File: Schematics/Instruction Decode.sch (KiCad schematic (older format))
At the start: 10 parts, among them U52 GLS29EE010, U53 GLS29EE010, U54 74F574, U55 74F574, U56 74F574

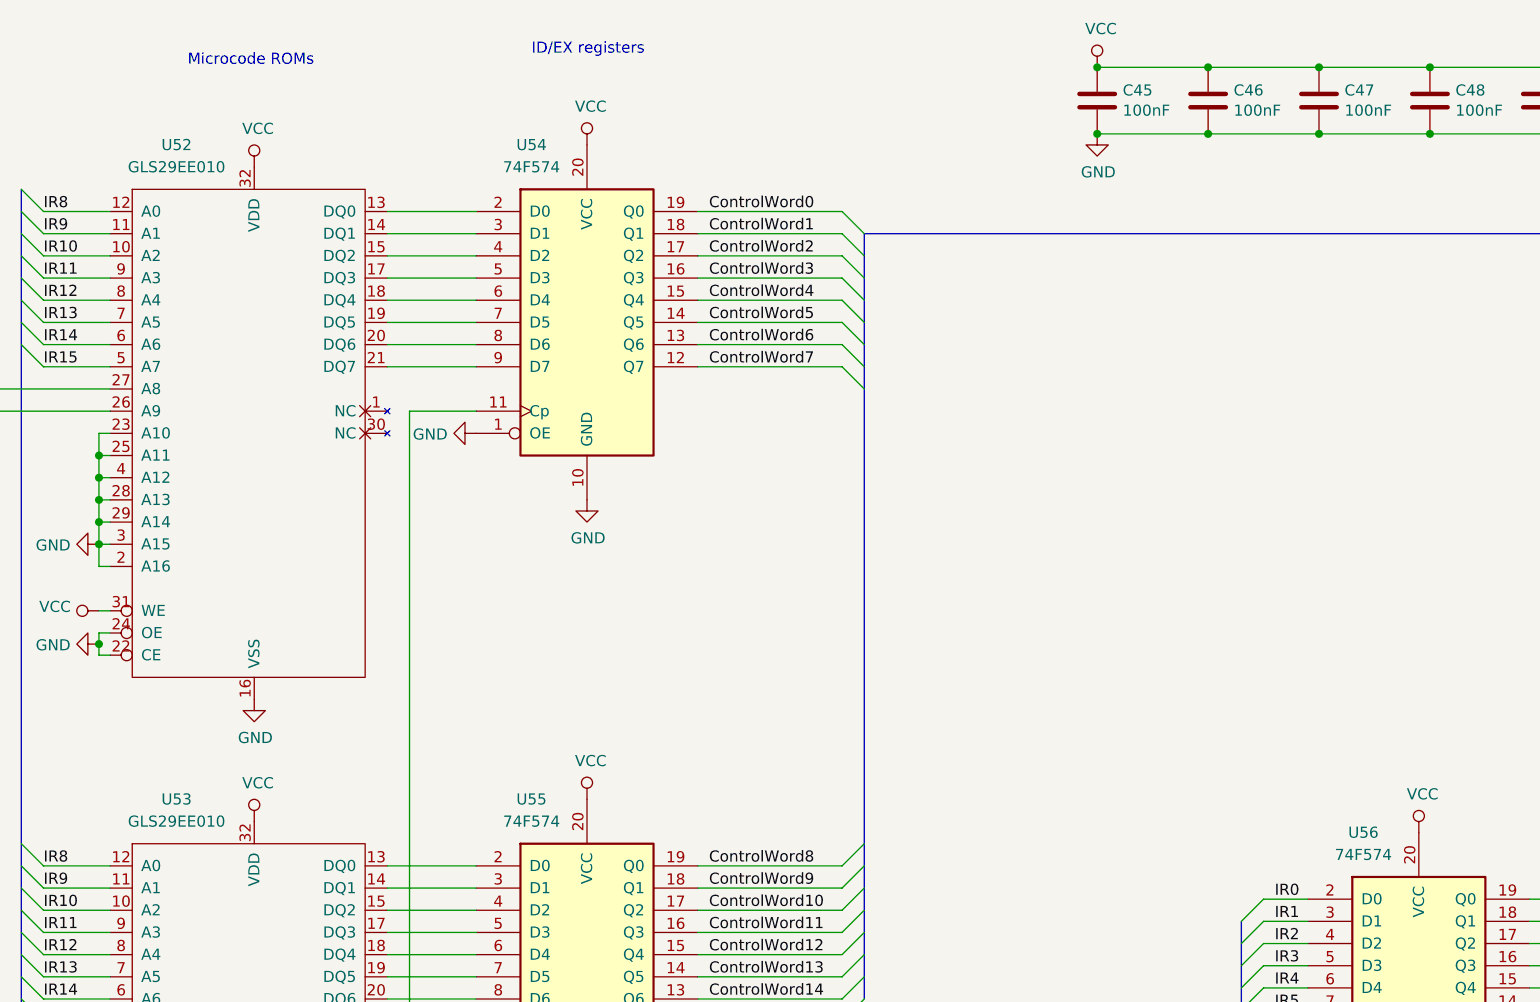
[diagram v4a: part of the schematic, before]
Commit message: Add unused IC units to Output Display to ensure no ICs are shared with other modules.
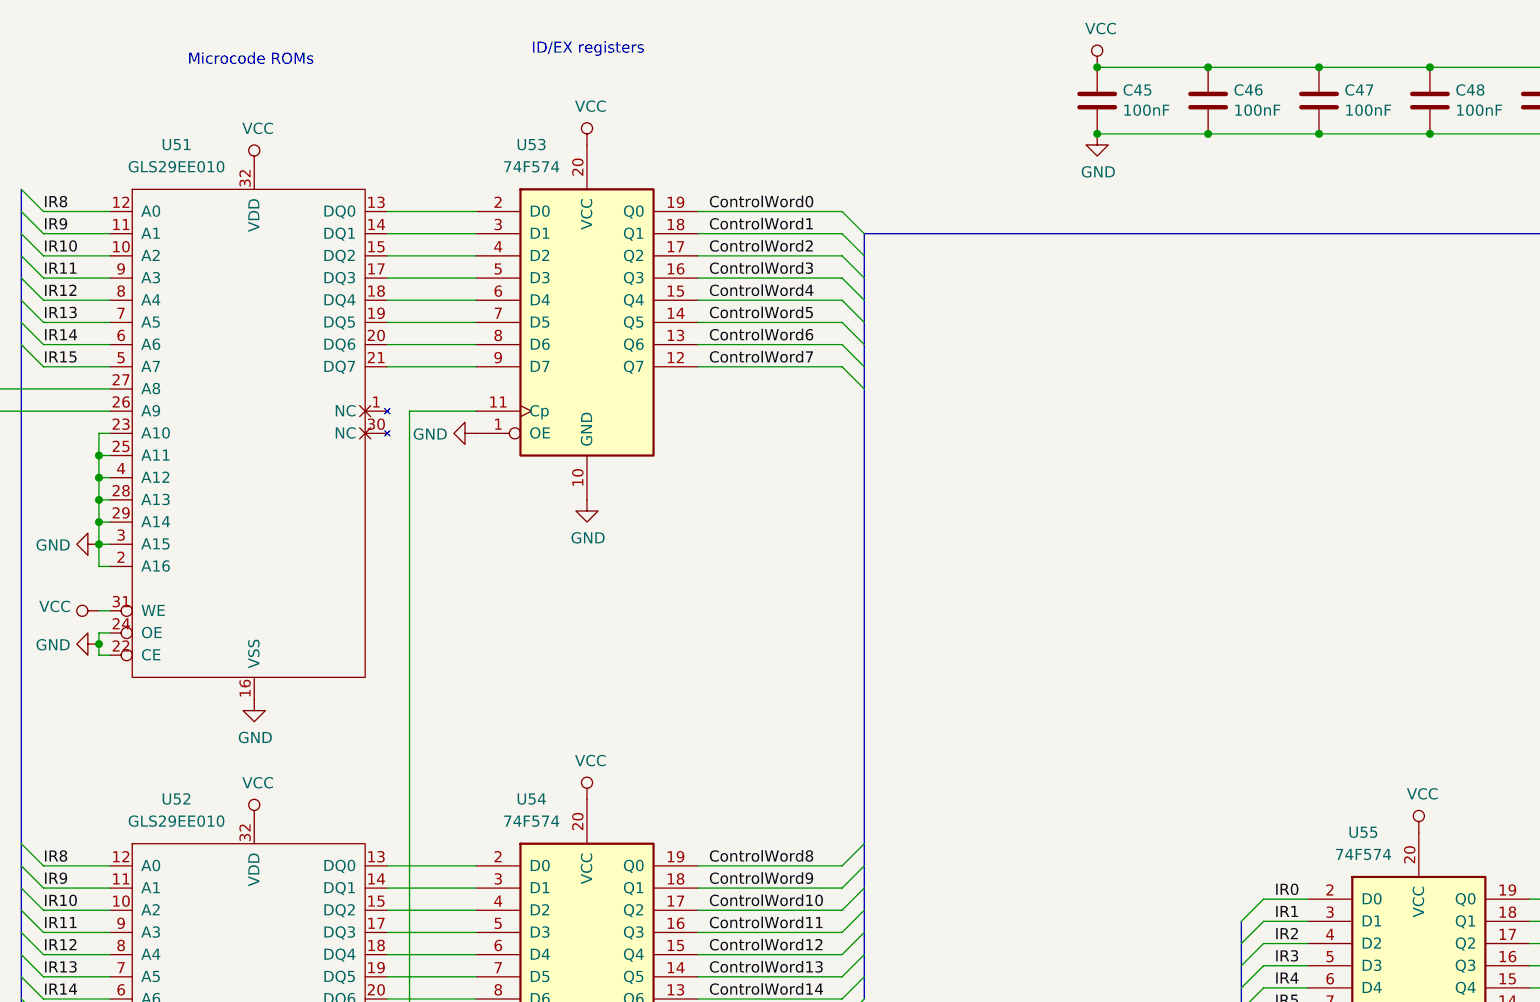
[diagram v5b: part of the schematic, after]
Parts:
- renumbered U52 to U51, U53 to U52, U54 to U53, U55 to U54, U56 to U55
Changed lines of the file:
@@
 P 2900 1250
 AR Path="/5D2C0AA0/5DB5EC09" Ref="U?"  Part="1"
-AR Path="/5D2C0B92/5DB5EC09" Ref="U52"  Part="1"
-F 0 "U52" H 2550 1450 50  0000 C CNN
+AR Path="/5D2C0B92/5DB5EC09" Ref="U51"  Part="1"
+F 0 "U51" H 2550 1450 50  0000 C CNN
 F 1 "GLS29EE010" H 2550 1350 50  0000 C CNN
 F 2 "Package_DIP:DIP-32_W15.24mm_Socket" H 2900 1250 50  0001 C CNN
@@
 P 2900 4200
 AR Path="/5D2C0AA0/5DB5EC5B" Ref="U?"  Part="1"
-AR Path="/5D2C0B92/5DB5EC5B" Ref="U53"  Part="1"
-F 0 "U53" H 2550 4400 50  0000 C CNN
+AR Path="/5D2C0B92/5DB5EC5B" Ref="U52"  Part="1"
+F 0 "U52" H 2550 4400 50  0000 C CNN
 F 1 "GLS29EE010" H 2550 4300 50  0000 C CNN
 F 2 "Package_DIP:DIP-32_W15.24mm_Socket" H 2900 4200 50  0001 C CNN
@@
 P 8150 4950
 AR Path="/5D2C14C3/5DB613F7" Ref="U?"  Part="1"
-AR Path="/5D2C0B92/5DB613F7" Ref="U56"  Part="1"
-F 0 "U56" H 7900 5750 50  0000 C CNN
+AR Path="/5D2C0B92/5DB613F7" Ref="U55"  Part="1"
+F 0 "U55" H 7900 5750 50  0000 C CNN
 F 1 "74F574" H 7900 5650 50  0000 C CNN
 F 2 "Package_DIP:DIP-20_W7.62mm" H 8150 4950 50  0001 C CNN
@@
 $EndComp
 $Comp
-L power:GND #PWR0213
+L power:GND #PWR0133
 U 1 1 5DB6758A
 P 8150 5750
-F 0 "#PWR0213" H 8150 5500 50  0001 C CNN
+F 0 "#PWR0133" H 8150 5500 50  0001 C CNN
 F 1 "GND" H 8155 5577 50  0000 C CNN
 F 2 "" H 8150 5750 50  0001 C CNN
@@
 $EndComp
 $Comp
-L power:VCC #PWR0214
+L power:VCC #PWR0132
 U 1 1 5DB6804E
 P 8150 4150
-F 0 "#PWR0214" H 8150 4000 50  0001 C CNN
+F 0 "#PWR0132" H 8150 4000 50  0001 C CNN
 F 1 "VCC" H 8167 4323 50  0000 C CNN
 F 2 "" H 8150 4150 50  0001 C CNN
@@
 ControlClock
 $Comp
-L power:GND #PWR0215
+L power:GND #PWR0131
 U 1 1 5DB73C30
 P 7650 5450
-F 0 "#PWR0215" H 7650 5200 50  0001 C CNN
+F 0 "#PWR0131" H 7650 5200 50  0001 C CNN
 F 1 "GND" V 7655 5322 50  0000 R CNN
 F 2 "" H 7650 5450 50  0001 C CNN
@@
 P 4400 1850
 AR Path="/5D2C14C3/5DB75B66" Ref="U?"  Part="1"
-AR Path="/5D2C0B92/5DB75B66" Ref="U54"  Part="1"
-F 0 "U54" H 4150 2650 50  0000 C CNN
+AR Path="/5D2C0B92/5DB75B66" Ref="U53"  Part="1"
+F 0 "U53" H 4150 2650 50  0000 C CNN
 F 1 "74F574" H 4150 2550 50  0000 C CNN
 F 2 "Package_DIP:DIP-20_W7.62mm" H 4400 1850 50  0001 C CNN
@@
 P 4400 4800
 AR Path="/5D2C14C3/5DB7864A" Ref="U?"  Part="1"
-AR Path="/5D2C0B92/5DB7864A" Ref="U55"  Part="1"
-F 0 "U55" H 4150 5600 50  0000 C CNN
+AR Path="/5D2C0B92/5DB7864A" Ref="U54"  Part="1"
+F 0 "U54" H 4150 5600 50  0000 C CNN
 F 1 "74F574" H 4150 5500 50  0000 C CNN
 F 2 "Package_DIP:DIP-20_W7.62mm" H 4400 4800 50  0001 C CNN
@@
 $EndComp
 $Comp
-L power:GND #PWR0216
+L power:GND #PWR0128
 U 1 1 5DB796AD
 P 4400 5600
-F 0 "#PWR0216" H 4400 5350 50  0001 C CNN
+F 0 "#PWR0128" H 4400 5350 50  0001 C CNN
 F 1 "GND" H 4405 5427 50  0000 C CNN
 F 2 "" H 4400 5600 50  0001 C CNN
@@
 $EndComp
 $Comp
-L power:GND #PWR0217
+L power:GND #PWR0126
 U 1 1 5DB79B03
 P 4400 2650
-F 0 "#PWR0217" H 4400 2400 50  0001 C CNN
+F 0 "#PWR0126" H 4400 2400 50  0001 C CNN
 F 1 "GND" H 4405 2477 50  0000 C CNN
 F 2 "" H 4400 2650 50  0001 C CNN
@@
 $EndComp
 $Comp
-L power:VCC #PWR0218
+L power:VCC #PWR0125
 U 1 1 5DB7A069
 P 4400 1050
-F 0 "#PWR0218" H 4400 900 50  0001 C CNN
+F 0 "#PWR0125" H 4400 900 50  0001 C CNN
 F 1 "VCC" H 4417 1223 50  0000 C CNN
 F 2 "" H 4400 1050 50  0001 C CNN
@@
 $EndComp
 $Comp
-L power:VCC #PWR0219
+L power:VCC #PWR0127
 U 1 1 5DB7A788
 P 4400 4000
-F 0 "#PWR0219" H 4400 3850 50  0001 C CNN
+F 0 "#PWR0127" H 4400 3850 50  0001 C CNN
 F 1 "VCC" H 4417 4173 50  0000 C CNN
 F 2 "" H 4400 4000 50  0001 C CNN
@@
 $EndComp
 $Comp
-L power:VCC #PWR0220
+L power:VCC #PWR0121
 U 1 1 5DB7ADC3
 P 2900 4100
-F 0 "#PWR0220" H 2900 3950 50  0001 C CNN
+F 0 "#PWR0121" H 2900 3950 50  0001 C CNN
 F 1 "VCC" H 2917 4273 50  0000 C CNN
 F 2 "" H 2900 4100 50  0001 C CNN
@@
 $EndComp
 $Comp
-L power:VCC #PWR0221
+L power:VCC #PWR0119
 U 1 1 5DB7B2F7
 P 2900 1150
-F 0 "#PWR0221" H 2900 1000 50  0001 C CNN
+F 0 "#PWR0119" H 2900 1000 50  0001 C CNN
 F 1 "VCC" H 2917 1323 50  0000 C CNN
 F 2 "" H 2900 1150 50  0001 C CNN
@@
 $EndComp
 $Comp
-L power:GND #PWR0222
+L power:GND #PWR0122
 U 1 1 5DB7B91A
 P 2900 6500
-F 0 "#PWR0222" H 2900 6250 50  0001 C CNN
+F 0 "#PWR0122" H 2900 6250 50  0001 C CNN
 F 1 "GND" H 2905 6327 50  0000 C CNN
 F 2 "" H 2900 6500 50  0001 C CNN
@@
 Connection ~ 3600 5200
 $Comp
-L power:GND #PWR0223
+L power:GND #PWR0124
 U 1 1 5DB80A57
 P 3900 5300
-F 0 "#PWR0223" H 3900 5050 50  0001 C CNN
+F 0 "#PWR0124" H 3900 5050 50  0001 C CNN
 F 1 "GND" V 3905 5172 50  0000 R CNN
 F 2 "" H 3900 5300 50  0001 C CNN
@@
 $EndComp
 $Comp
-L power:GND #PWR0224
+L power:GND #PWR0123
 U 1 1 5DB8100B
 P 3900 2350
-F 0 "#PWR0224" H 3900 2100 50  0001 C CNN
+F 0 "#PWR0123" H 3900 2100 50  0001 C CNN
 F 1 "GND" V 3905 2222 50  0000 R CNN
 F 2 "" H 3900 2350 50  0001 C CNN
@@
 	2200 6300 2250 6300
 $Comp
-L power:GND #PWR0225
+L power:GND #PWR0118
 U 1 1 5DBD4428
 P 2200 6250
-F 0 "#PWR0225" H 2200 6000 50  0001 C CNN
+F 0 "#PWR0118" H 2200 6000 50  0001 C CNN
 F 1 "GND" V 2205 6122 50  0000 R CNN
 F 2 "" H 2200 6250 50  0001 C CNN
@@
 	2200 3350 2250 3350
 $Comp
-L power:GND #PWR0226
+L power:GND #PWR0115
 U 1 1 5DBE64D4
 P 2200 3300
-F 0 "#PWR0226" H 2200 3050 50  0001 C CNN
+F 0 "#PWR0115" H 2200 3050 50  0001 C CNN
 F 1 "GND" V 2205 3172 50  0000 R CNN
 F 2 "" H 2200 3300 50  0001 C CNN
@@
 	2200 3300 2200 3350
 $Comp
-L power:VCC #PWR0227
+L power:VCC #PWR0117
 U 1 1 5DBEAA53
 P 2200 6100
-F 0 "#PWR0227" H 2200 5950 50  0001 C CNN
+F 0 "#PWR0117" H 2200 5950 50  0001 C CNN
 F 1 "VCC" V 2218 6227 50  0000 L CNN
 F 2 "" H 2200 6100 50  0001 C CNN
@@
 	2250 6100 2200 6100
 $Comp
-L power:VCC #PWR0228
+L power:VCC #PWR0114
 U 1 1 5DBEFE69
 P 2200 3150
-F 0 "#PWR0228" H 2200 3000 50  0001 C CNN
+F 0 "#PWR0114" H 2200 3000 50  0001 C CNN
 F 1 "VCC" V 2218 3277 50  0000 L CNN
 F 2 "" H 2200 3150 50  0001 C CNN
@@
 	2200 2450 2200 2550
 $Comp
-L power:GND #PWR0229
+L power:GND #PWR0113
 U 1 1 5DC141C5
 P 2200 2850
-F 0 "#PWR0229" H 2200 2600 50  0001 C CNN
+F 0 "#PWR0113" H 2200 2600 50  0001 C CNN
 F 1 "GND" V 2205 2722 50  0000 R CNN
 F 2 "" H 2200 2850 50  0001 C CNN
@@
 	2200 5400 2200 5500
 $Comp
-L power:GND #PWR0230
+L power:GND #PWR0116
 U 1 1 5DC266E6
 P 2200 5800
-F 0 "#PWR0230" H 2200 5550 50  0001 C CNN
+F 0 "#PWR0116" H 2200 5550 50  0001 C CNN
 F 1 "GND" V 2205 5672 50  0000 R CNN
 F 2 "" H 2200 5800 50  0001 C CNN
@@
 	1650 2250 2250 2250
 $Comp
-L power:GND #PWR0231
+L power:GND #PWR0120
 U 1 1 5DC7501F
 P 2900 3550
-F 0 "#PWR0231" H 2900 3300 50  0001 C CNN
+F 0 "#PWR0120" H 2900 3300 50  0001 C CNN
 F 1 "GND" H 2905 3377 50  0000 C CNN
 F 2 "" H 2900 3550 50  0001 C CNN
@@
 P 6700 700
 AR Path="/5D2C0761/5DC56D8C" Ref="#PWR?"  Part="1"
-AR Path="/5D2C0B92/5DC56D8C" Ref="#PWR0232"  Part="1"
-F 0 "#PWR0232" H 6700 550 50  0001 C CNN
+AR Path="/5D2C0B92/5DC56D8C" Ref="#PWR0129"  Part="1"
+F 0 "#PWR0129" H 6700 550 50  0001 C CNN
 F 1 "VCC" H 6717 873 50  0000 C CNN
 F 2 "" H 6700 700 50  0001 C CNN
@@
 P 6700 1000
 AR Path="/5D2C0761/5DC56D86" Ref="#PWR?"  Part="1"
-AR Path="/5D2C0B92/5DC56D86" Ref="#PWR0233"  Part="1"
-F 0 "#PWR0233" H 6700 750 50  0001 C CNN
+AR Path="/5D2C0B92/5DC56D86" Ref="#PWR0130"  Part="1"
+F 0 "#PWR0130" H 6700 750 50  0001 C CNN
 F 1 "GND" H 6705 827 50  0000 C CNN
 F 2 "" H 6700 1000 50  0001 C CNN

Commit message: Add unused IC units to Data RAM to ensure no ICs are shared with other modules.
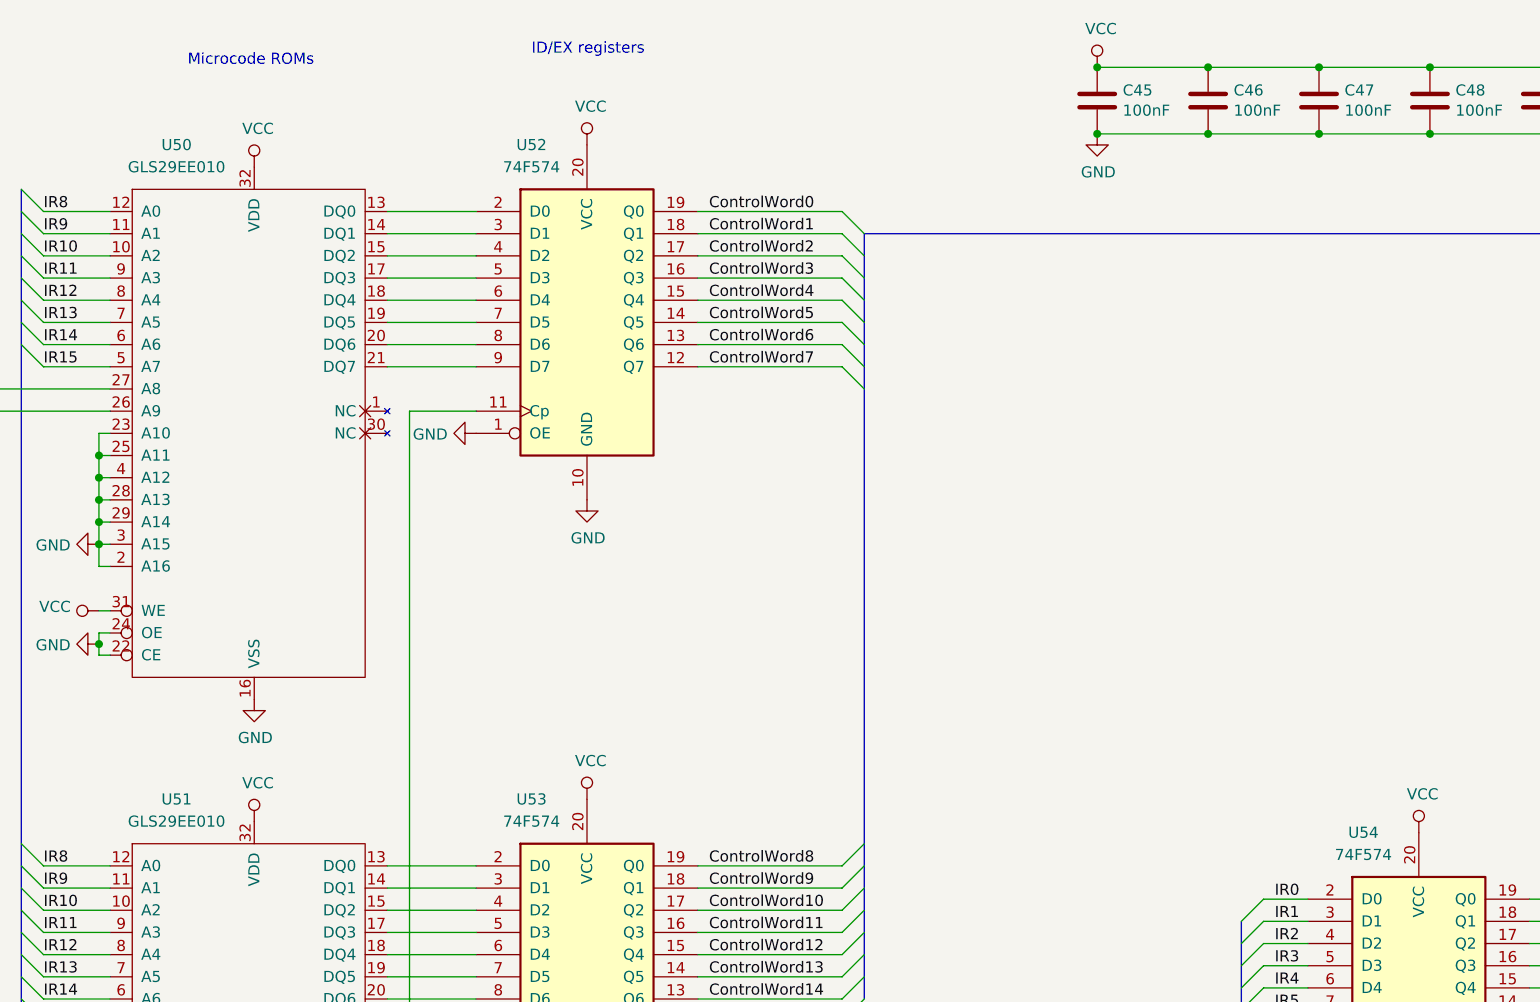
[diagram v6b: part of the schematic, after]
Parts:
- renumbered U51 to U50, U52 to U51, U53 to U52, U54 to U53, U55 to U54
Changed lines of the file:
@@
 P 2900 1250
 AR Path="/5D2C0AA0/5DB5EC09" Ref="U?"  Part="1"
-AR Path="/5D2C0B92/5DB5EC09" Ref="U51"  Part="1"
-F 0 "U51" H 2550 1450 50  0000 C CNN
+AR Path="/5D2C0B92/5DB5EC09" Ref="U50"  Part="1"
+F 0 "U50" H 2550 1450 50  0000 C CNN
 F 1 "GLS29EE010" H 2550 1350 50  0000 C CNN
 F 2 "Package_DIP:DIP-32_W15.24mm_Socket" H 2900 1250 50  0001 C CNN
@@
 P 2900 4200
 AR Path="/5D2C0AA0/5DB5EC5B" Ref="U?"  Part="1"
-AR Path="/5D2C0B92/5DB5EC5B" Ref="U52"  Part="1"
-F 0 "U52" H 2550 4400 50  0000 C CNN
+AR Path="/5D2C0B92/5DB5EC5B" Ref="U51"  Part="1"
+F 0 "U51" H 2550 4400 50  0000 C CNN
 F 1 "GLS29EE010" H 2550 4300 50  0000 C CNN
 F 2 "Package_DIP:DIP-32_W15.24mm_Socket" H 2900 4200 50  0001 C CNN
@@
 P 8150 4950
 AR Path="/5D2C14C3/5DB613F7" Ref="U?"  Part="1"
-AR Path="/5D2C0B92/5DB613F7" Ref="U55"  Part="1"
-F 0 "U55" H 7900 5750 50  0000 C CNN
+AR Path="/5D2C0B92/5DB613F7" Ref="U54"  Part="1"
+F 0 "U54" H 7900 5750 50  0000 C CNN
 F 1 "74F574" H 7900 5650 50  0000 C CNN
 F 2 "Package_DIP:DIP-20_W7.62mm" H 8150 4950 50  0001 C CNN
@@
 P 4400 1850
 AR Path="/5D2C14C3/5DB75B66" Ref="U?"  Part="1"
-AR Path="/5D2C0B92/5DB75B66" Ref="U53"  Part="1"
-F 0 "U53" H 4150 2650 50  0000 C CNN
+AR Path="/5D2C0B92/5DB75B66" Ref="U52"  Part="1"
+F 0 "U52" H 4150 2650 50  0000 C CNN
 F 1 "74F574" H 4150 2550 50  0000 C CNN
 F 2 "Package_DIP:DIP-20_W7.62mm" H 4400 1850 50  0001 C CNN
@@
 P 4400 4800
 AR Path="/5D2C14C3/5DB7864A" Ref="U?"  Part="1"
-AR Path="/5D2C0B92/5DB7864A" Ref="U54"  Part="1"
-F 0 "U54" H 4150 5600 50  0000 C CNN
+AR Path="/5D2C0B92/5DB7864A" Ref="U53"  Part="1"
+F 0 "U53" H 4150 5600 50  0000 C CNN
 F 1 "74F574" H 4150 5500 50  0000 C CNN
 F 2 "Package_DIP:DIP-20_W7.62mm" H 4400 4800 50  0001 C CNN
